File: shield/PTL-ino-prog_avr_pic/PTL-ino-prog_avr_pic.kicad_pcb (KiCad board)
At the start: 2 copper layers, 55.9 x 66 mm, 30 parts, among them P1 CONN_8, P2 CONN_6, P3 CONN_10, P4 CONN_8, P5 CONN_3X2, P6 CONN_01X02, P7 CONN_6, Q1 BC548, U1 PIC16F1455, U2 ATmega328

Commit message: added quartz
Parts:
- removed ?: , PTL-ino:PTL
- removed ?: , PTL-ino:PTL_mini
- removed G***: LOGO, PTL-ino:Logo_silk_CC-BY-SA_10x4.5mm
- removed RST: RST, Buttons_Switches_ThroughHole:SW_PUSH_SMALL
- added C5: 20pF, Capacitors_SMD:C_1206, F.Cu at (121.1, 66.8)
- added C6: 20pF, Capacitors_SMD:C_1206, F.Cu at (121.1, 70.6)
- added RST1: RST, PTL-ino:SW_PUSH_SMALL, F.Cu at (123.1, 58.7)
- added Y1: Crystal, Crystals:Crystal_HC50-U_Vertical, F.Cu at (121.9, 87.5)
- USR1, USR2: footprint Buttons_Switches_ThroughHole:SW_PUSH_SMALL -> PTL-ino:SW_PUSH_SMALL
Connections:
- U2 pad 9: Net-(U1-Pad3) -> Net-(C5-Pad2)
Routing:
- net Net-(C5-Pad2): track 0.00 -> 37.2 mm
- net /AREF: track 35.0 -> 57.3 mm
- net Net-(C6-Pad1): track 0.00 -> 21.1 mm, vias 0 -> 1
- net GND: track 222.1 -> 231.8 mm
- net /11: track 83.8 -> 88.9 mm
- net Net-(U1-Pad3): track 28.1 -> 26.6 mm
- net /12: track 72.6 -> 73.3 mm
- net /~RST: track 80.1 -> 79.6 mm
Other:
- board text removed: "PTL-ino programmer shield"

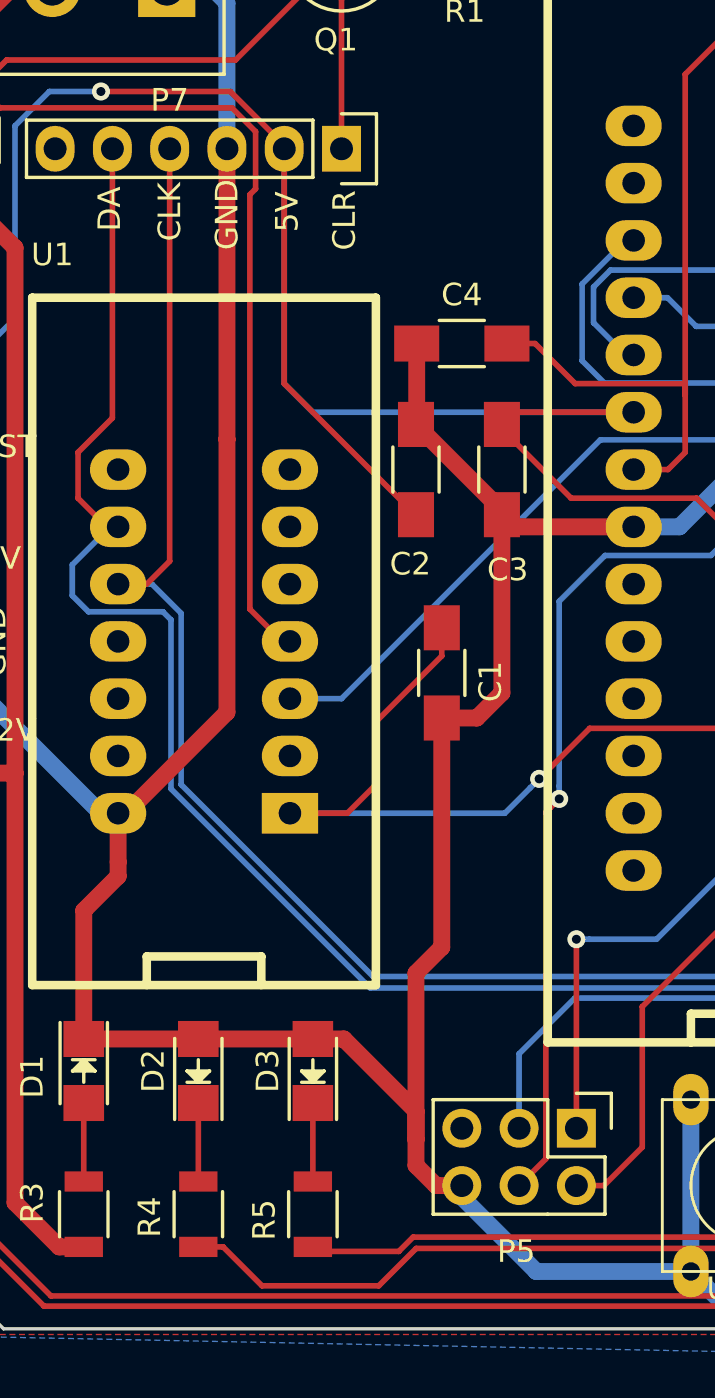
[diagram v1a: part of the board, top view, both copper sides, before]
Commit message: Added PTL footprint
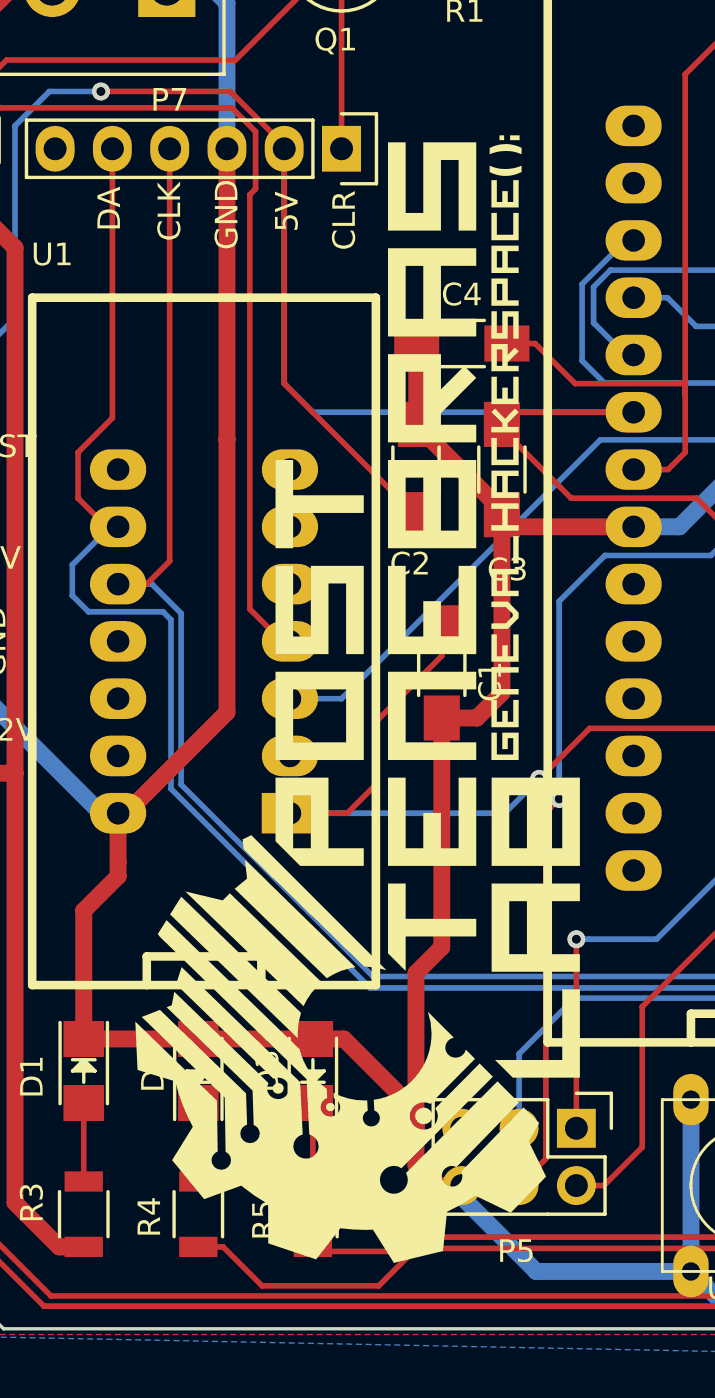
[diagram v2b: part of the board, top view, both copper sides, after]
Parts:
- added ?: , PTL-ino:PTL_mini, B.Cu at (93.0, 112.9)
- added ?: , PTL-ino:PTL, F.Cu at (84.6, 116.7)
- added G***: LOGO, PTL-ino:Logo_silk_CC-BY-SA_10x4.5mm, B.Cu at (97.8, 71.2)
